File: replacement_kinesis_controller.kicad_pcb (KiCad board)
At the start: 2 copper layers, 99.1 x 86.4 mm, 115 parts, among them CN1 USB_general, CN2 Micro-USB, CN3 Mini-USB, CN4 USB_general, K1 CONN_3, K2 CONN_3, K3 CONN_3, K4 CONN_3, P1 CONN_3X2, P10 CONN_8, P11 CONN_5, P12 CONN_5, P13 CONN_6, P14 CONN_8, P15 CONN_5X2, P16 CONN_16, P17 CONN_16, P18 POWER, P19 PCM, P2 CONN_13, P20 UART, P21 SPI, P22 IO, P23 SMIRF, P24 CONN_2, P25 USB, P3 CONN_13, P4 CONN_10, P5 CONN_10, P6 CONN_13, P7 CONN_13, P8 CONN_5X2, P9 CONN_6, Q1 MOS_P, Q2 MOS_N, Q3 MOS_P, SW1 SW_PUSH, SW2 SW_PUSH, SW3 SPST, SW4 SPST, U1 MCP23018-E, U2 WS2811_RGB_LED, U3 WS2811_RGB_LED, U4 WS2811_RGB_LED, U5 WS2811_RGB_LED, U6 ATmega32U4, U7 WT12-A, U8 MCP73832, U9 MIC5504, X1 16MHz

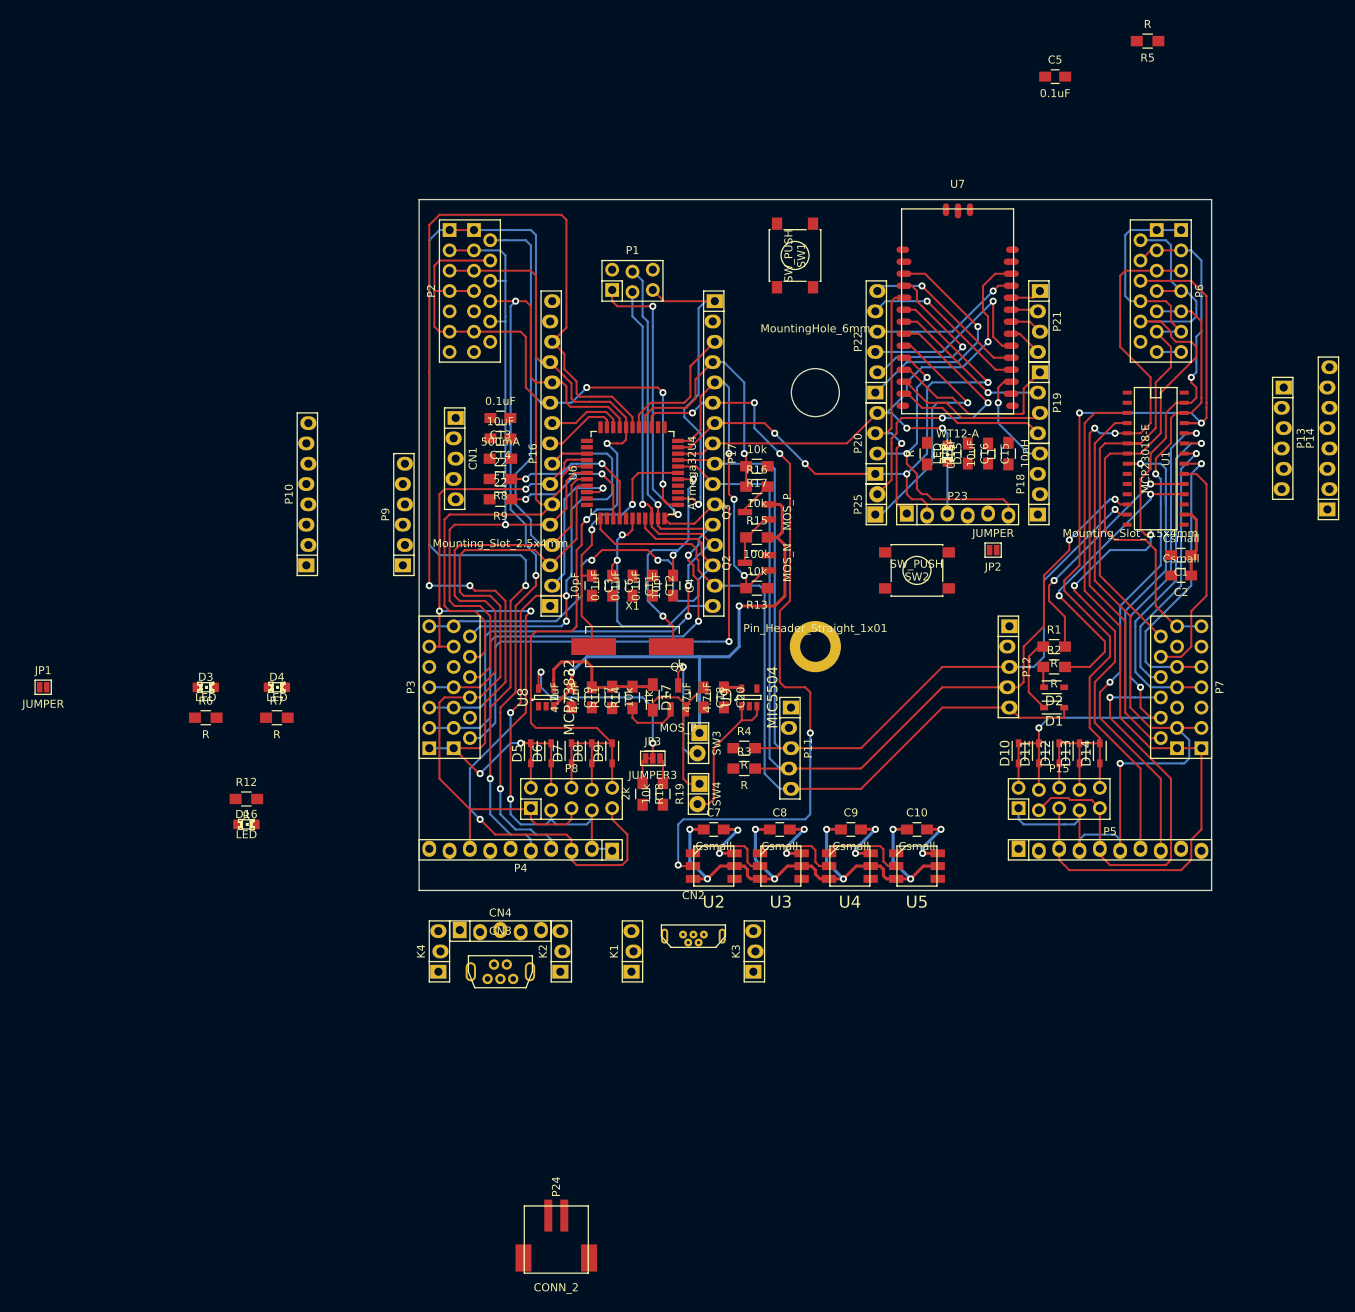
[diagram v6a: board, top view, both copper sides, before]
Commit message: Update bom and add a bunch of layout stuff
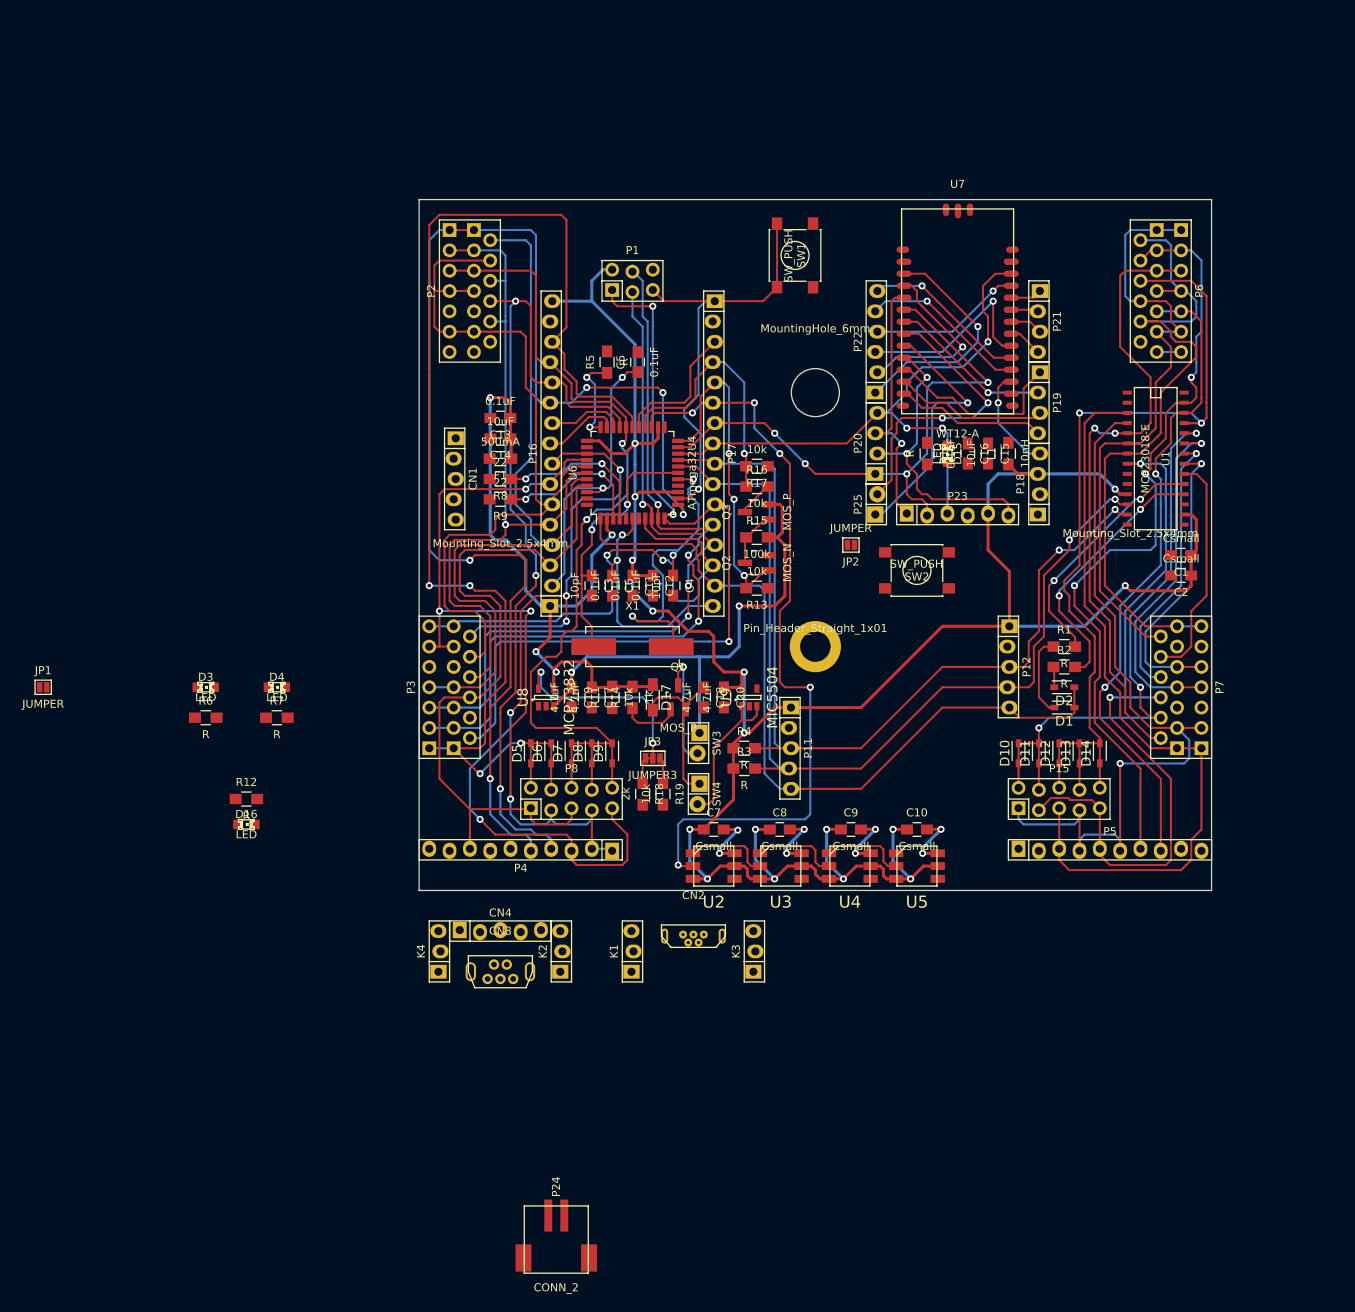
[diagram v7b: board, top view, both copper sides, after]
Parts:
- removed P10, P14: CONN_8, replacement_kinesis_controller:Pin_Header_Staggered_Straight_1x08
- removed P13, P9: CONN_6, replacement_kinesis_controller:Pin_Header_Staggered_Straight_1x06
- moved R5 78.6 mm to (97.2, 63.5), turned to 90 degrees
- moved C5 63.2 mm to (101.0, 63.5), turned to 90 degrees
- moved JP2 17.8 mm to (127.6, 86.4)
- moved CN1 2.54 mm to (78.1, 78.1)
- moved D1 1.27 mm to (154.3, 106.7)
- moved D2 1.27 mm to (154.3, 104.1)
- moved R1 1.27 mm to (154.3, 99.1)
- moved R2 1.27 mm to (154.3, 101.6)
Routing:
- net VCC: track 85.1 -> 307.6 mm, vias 8 -> 16
- net +5V: track 18.1 -> 85.4 mm, vias 0 -> 4
- net AREF: track 19.1 -> 36.4 mm, vias 1 -> 2
- net RESET: track 39.8 -> 54.7 mm
- net PE2: track 0.00 -> 11.1 mm, vias 0 -> 2
- net Net-(C4-Pad1): track 32.0 -> 40.3 mm
- net PE6: track 93.5 -> 97.7 mm
- net COL_5: track 116.2 -> 112.4 mm, vias 4 -> 5
- net INTB: track 36.8 -> 33.2 mm
- net ROW_L5: track 119.0 -> 115.8 mm
- net ROW_L0: track 62.2 -> 64.9 mm
- net ROW_L7: track 160.4 -> 162.7 mm
- net GPA5: track 115.5 -> 113.9 mm
- net GPA7: track 100.0 -> 98.4 mm
- net COL_9: track 79.4 -> 80.6 mm
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
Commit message: A bunch more rejiggering
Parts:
- moved JP1 78.1 mm to (93.3, 63.5), turned to 270 degrees
- moved R6 76.9 mm to (94.6, 47.6), turned to 90 degrees
- moved D3 75.6 mm to (97.2, 47.6), turned to 270 degrees
- moved D16 48.7 mm to (99.7, 111.1), turned to 90 degrees
- moved R12 44.1 mm to (95.2, 109.2)
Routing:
- net CHARGE_STATUS: track 17.1 -> 113.2 mm, vias 0 -> 5
- net +5V: track 85.4 -> 112.6 mm, vias 4 -> 6
- net Net-(JP3-Pad1): track 29.6 -> 34.3 mm
- net ROW_L5: track 115.8 -> 111.5 mm
- net Net-(Q1-PadD): track 14.8 -> 11.3 mm
- net Net-(D16-Pad2): track 0.00 -> 3.45 mm
- net VCC: track 307.6 -> 309.4 mm
- net PD3: track 73.7 -> 74.8 mm
- net LED_DATA: track 96.2 -> 95.3 mm
